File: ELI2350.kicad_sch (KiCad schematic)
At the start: 55 parts, among them J3 Conn_01x03_Pin, U1 W25Q128JVPIQ, U2 FLASH or PSRAM, U3 TPS62163DSG, U4 TLV76733DRVR, U5 RP235x-B, U6 TLV76733DRVR, Y1 CM4012M00012001

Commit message: alpha
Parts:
- added H1, H2: MountingHole_Pad, MountingHole:MountingHole_2.2mm_M2_Pad, symbol Mechanical:MountingHole_Pad
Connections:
- net GND: now also CN2.2, CN3.2, H1.1
- net GPIO1: no longer CN2.2
- net GPIO20: no longer CN3.1
- net GPIO21: now also CN3.1; no longer CN3.2
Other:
- note added: "https://jlcpcb.com/parts/componentSearch?searchTxt=pogo"

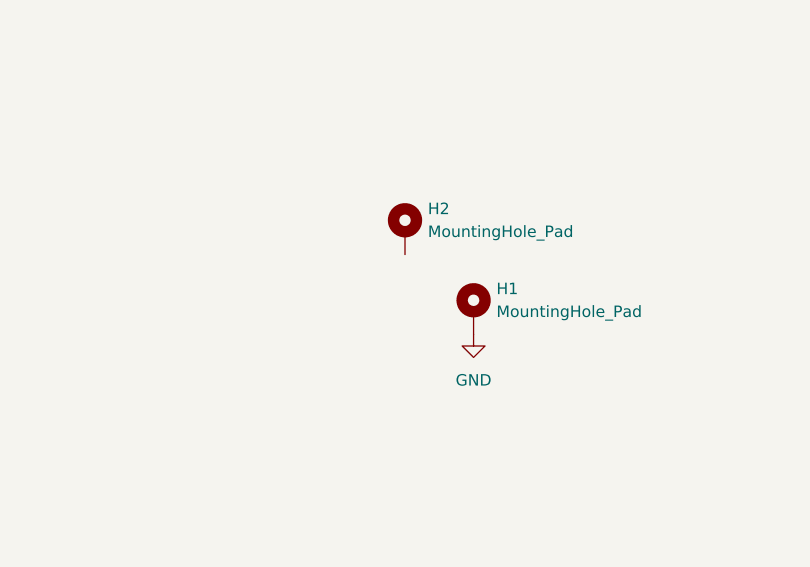
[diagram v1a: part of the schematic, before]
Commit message: dock and near finished compute board
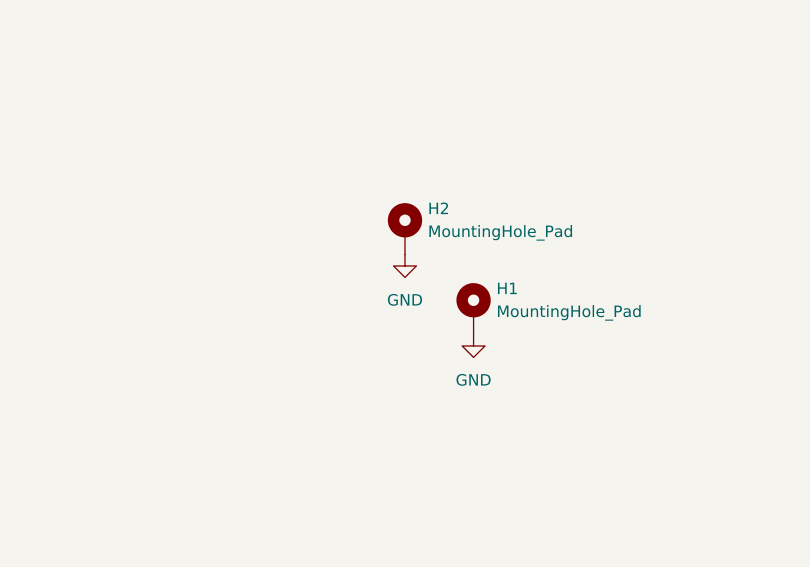
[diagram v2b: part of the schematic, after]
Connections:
- net GND: now also H2.1
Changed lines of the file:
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@@
+	)
+	(symbol
+		(lib_name "GND_16")
+		(lib_id "power:GND")
+		(at 90.17 133.35 0)
+		(unit 1)
+		(exclude_from_sim no)
+		(in_bom yes)
+		(on_board yes)
+		(dnp no)
+		(fields_autoplaced yes)
+		(property "Reference" "#PWR056"
+			(at 90.17 139.7 0)
+			(effects
+				(font
+					(size 1.27 1.27)
+				)
+				(hide yes)
+			)
+		)
+		(property "Value" "GND"
+			(at 90.17 138.43 0)
+			(effects
+				(font
+					(size 1.27 1.27)
+				)
+			)
+		)
+		(property "Footprint" ""
+			(at 90.17 133.35 0)
+			(effects
+				(font
+					(size 1.27 1.27)
+				)
+				(hide yes)
+			)
+		)
+		(property "Datasheet" ""
+			(at 90.17 133.35 0)
+			(effects
+				(font
+					(size 1.27 1.27)
+				)
+				(hide yes)
+			)
+		)
+		(property "Description" "Power symbol creates a global label with name \"GND\" , ground"
+			(at 90.17 133.35 0)
+			(effects
+				(font
+					(size 1.27 1.27)
+				)
+				(hide yes)
+			)
+		)
+		(pin "1"
+		)
+		(instances
+			(project ""
+				(path "/019f2816-6bfb-4531-95b3-45f73cf5fc4b"
+					(reference "#PWR056")
+					(unit 1)
+				)
+			)
+		)
 	)
 	(symbol

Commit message: doc pre-reroute
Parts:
- added TP1, TP2, TP3, TP4, TP5, TP6: TestPoint, TestPoint:TestPoint_Pad_1.5x1.5mm, symbol Connector:TestPoint
- CN1: JLC (none) -> C22390096; Supplier Part C22390096 -> (none)
- CN2, CN3: JLC (none) -> C3029422; Supplier Part C3029422 -> (none)
- SW1, SW2: JLC (none) -> C380198; Supplier Part C380198 -> (none)
- U1: JLC (none) -> C190862; LCSC C190862 -> (none)
- U3: JLC (none) -> C97534
- U4, U6: JLC (none) -> C2848334
- U5: JLC (none) -> C42415655
- Y1: JLC (none) -> C7294611
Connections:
- net +1.1V: now also TP5.1
- net +12V: now also TP1.1
- net +3V3: now also TP3.1
- net +3V3_SIG: now also TP4.1
- net +5V: now also TP2.1
- net GPIO2: now also TP6.1
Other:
- note removed: "add debug connector on back"
- note removed: "https://jlcpcb.com/parts/componentSearch?searchTxt=pogo"

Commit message: bboard
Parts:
- removed SW1, SW2: ~, emutelab:KEY-SMD_SKTDLHE010, symbol emutelab:SKTDLHE010
- added SW1, SW3: ~, emutelab:SW-SMD_4P-L3.5-W2.9-P1.30-LS4.8, symbol emutelab:SKSCLAE010
- C23: footprint Capacitor_SMD:C_0603_1608Metric -> Capacitor_SMD:C_0805_2012Metric
- Y1: JLC C7294611 -> C7294610; LCSC C7294611 -> C7294610
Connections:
- net GND: now also SW1.3, SW1.4, SW3.3, SW3.4
- net ~{BOOTSEL}: now also SW3.1
- net ~{RESET}: now also SW1.2
- no-connect marks 8 -> 10
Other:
- moved on the sheet: H1, H2
